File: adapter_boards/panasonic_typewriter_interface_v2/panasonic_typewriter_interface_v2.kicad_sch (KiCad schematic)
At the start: 47 parts, among them J1 KMDGX-8S-AS, J2 Conn_02x03_Odd_Even, J3 Conn_01x06_MountingPin, J4 Conn_01x08_MountingPin, J5 Conn_01x04_MountingPin, J6 Conn_01x09_Socket, J7 Conn_01x09_Socket, J8 Conn_01x10_Pin, SW1 SW_SPDT, SW2 SW_Push

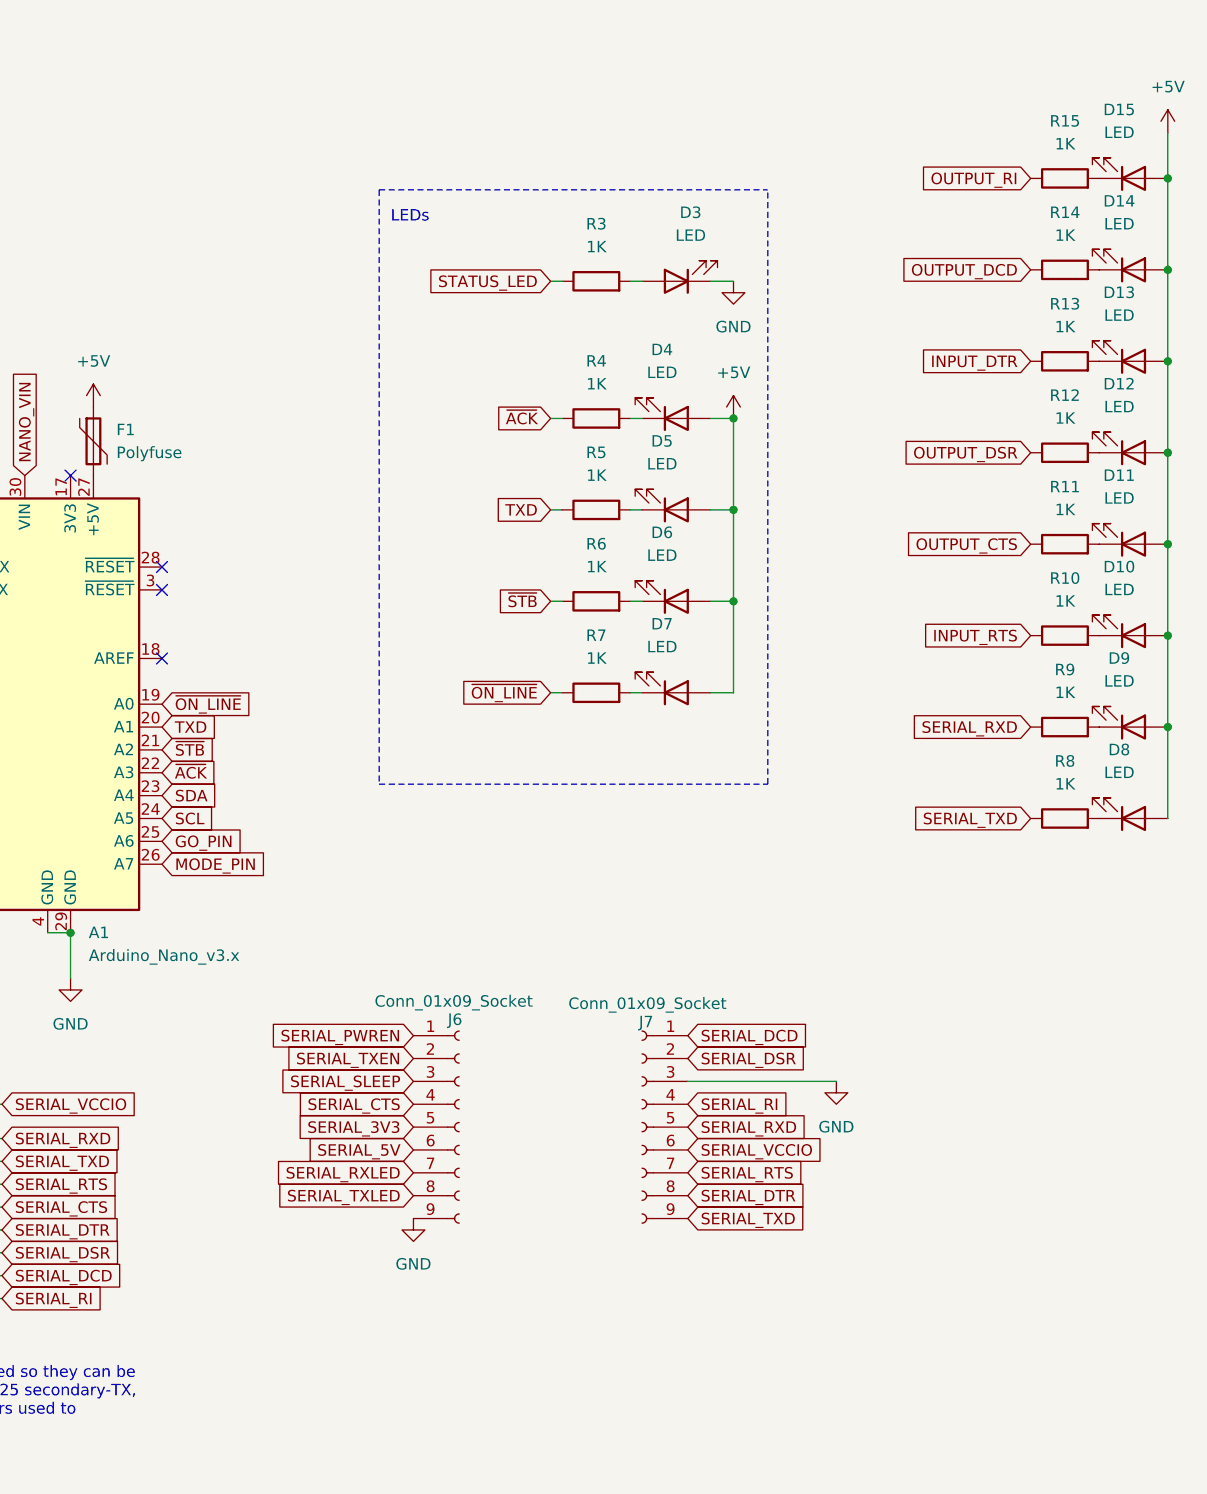
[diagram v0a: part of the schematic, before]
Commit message: Added DE-9 connector
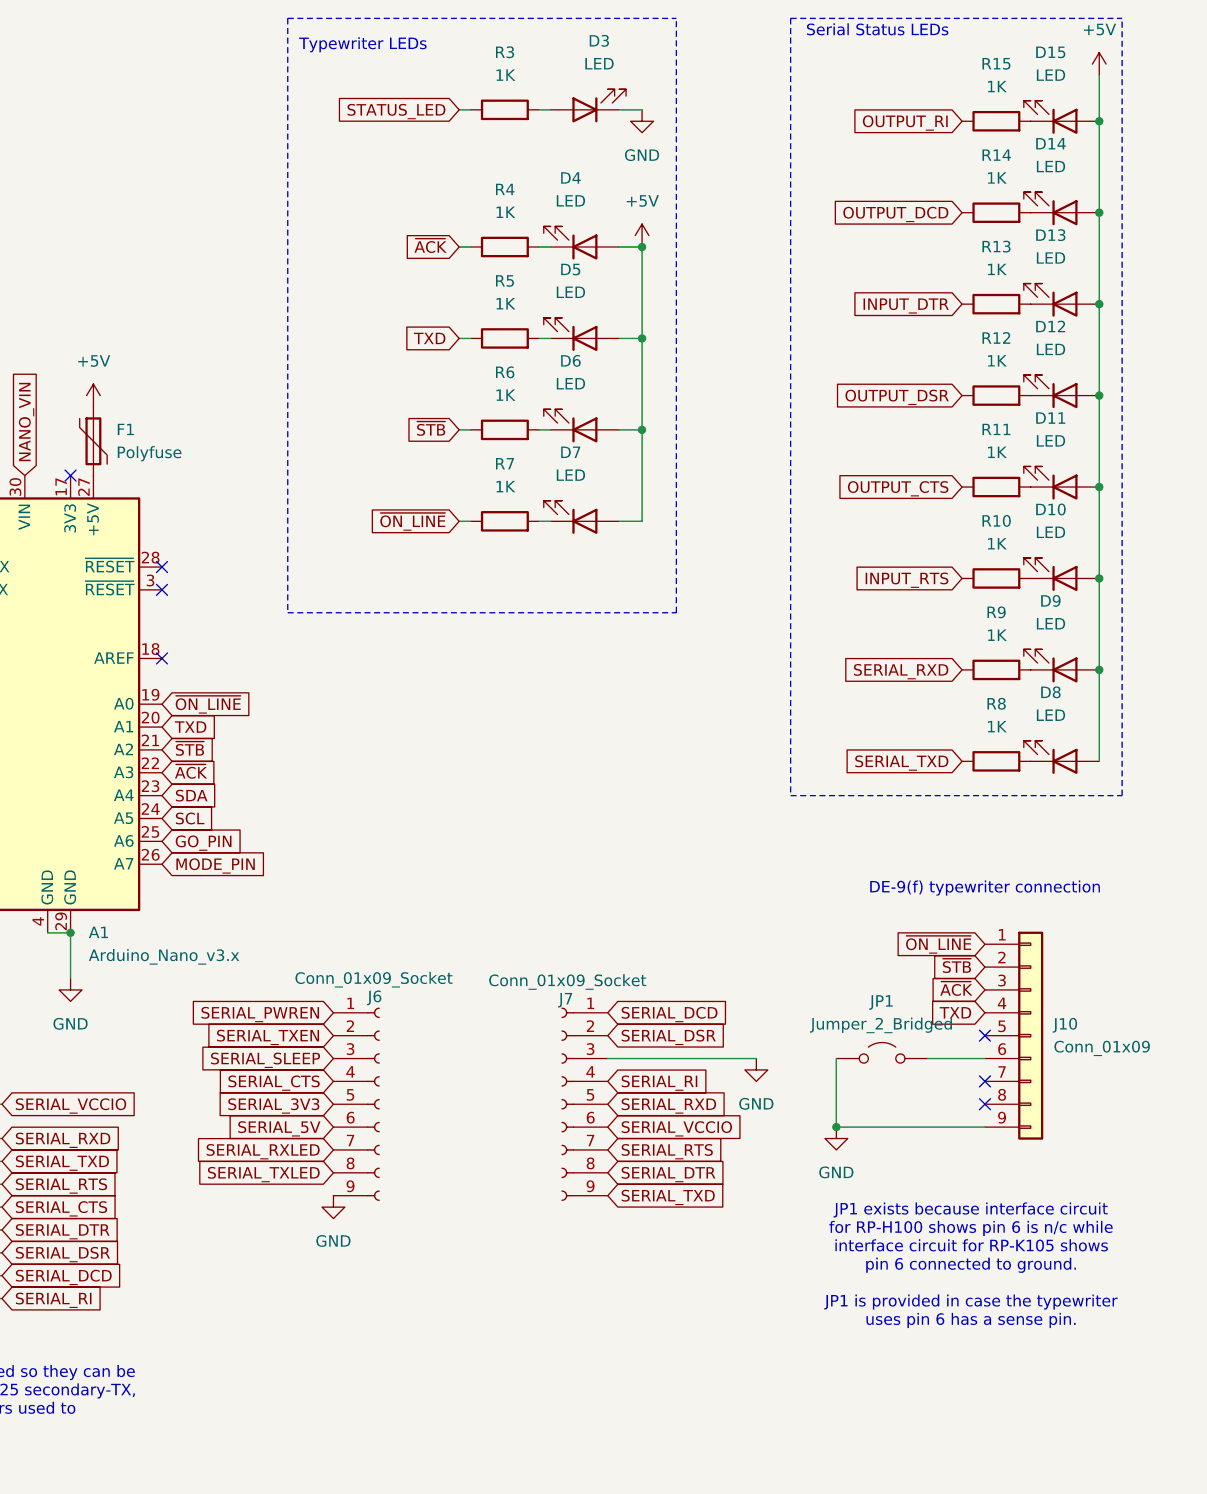
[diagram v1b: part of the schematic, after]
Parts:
- added J10: Conn_01x09, Connector_Dsub:DSUB-9_Female_EdgeMount_P2.77mm, symbol Connector_Generic:Conn_01x09
- added JP1: Jumper_2_Bridged, Jumper:SolderJumper-2_P1.3mm_Open_RoundedPad1.0x1.5mm, symbol Jumper:Jumper_2_Open
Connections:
- net GND: now also J10.9 (Pin_9), JP1.1 (A)
- net TXD: now also J10.4 (Pin_4)
- net ~{ACK}: now also J10.3 (Pin_3)
- net ~{ON_LINE}: now also J10.1 (Pin_1)
- net ~{STB}: now also J10.2 (Pin_2)
- new net: J10.6 (Pin_6), JP1.2 (B)
- no-connect marks 8 -> 11
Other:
- note added: "DE-9(f) typewriter connection"
- note added: "JP1 exists because interface circuit for RP-H100 shows pin 6 is n/c while interface circuit for RP-K105 shows pin 6 connected to ground. JP1 is provided in case the typewriter uses pin 6 has a sense pin."
- note added: "Serial Status LEDs"
- note added: "Typewriter LEDs"
- note removed: "LEDs"
- moved on the sheet: D10, D11, D12, D13, D14, D15, D3, D4, D5, D6, D7, D8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
